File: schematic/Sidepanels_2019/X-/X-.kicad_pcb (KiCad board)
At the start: 2 copper layers, 327.5 x 83.1 mm, 33 parts, among them J1 Conn_01x04, J2 Conn_01x02

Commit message: First attempt at modifying to all Spectrolabs.  NOT COMPLETE
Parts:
- removed D1, D10, D11, D12, D13, D14, D2, D3, D4, D5, D6, D7, D8, D9: D_Schottky, CySat footprints:Toshiba_CUS08F30
- removed the SC1 at (206.5, 125.5)
- removed SC10, SC11, SC12, SC13, SC14, SC15, SC16, SC8, SC9: Solar_Cell, CySat footprints:TriSelectSolarPanel
- removed the SC2 at (81.2, 125.6)
- added SC3: Solar_Cell, CySat_Solar:Spectrolab, F.Cu at (191.8, 143.5)
- added SC4: Solar_Cell, CySat_Solar:Spectrolab, F.Cu at (370.8, 142.2)
- SC5, SC6, SC7: footprint CySat footprints:TriSelectSolarPanel -> CySat_Solar:Spectrolab
- moved SC7 115.9 mm to (279.4, 143.5), turned to 90 degrees
- moved D15 94.2 mm to (141.3, 180.7)
- moved J1 94.2 mm to (92.8, 149.1)
- moved J2 94.2 mm to (92.8, 138.1)
- moved SC1 91.1 mm to (102.9, 144.8)
- moved SC2 89.1 mm to (147.3, 142.2)
- moved SC5 72.7 mm to (234.9, 143.5), turned to 90 degrees
- moved SC6 61.7 mm to (325.0, 142.2)
- renumbered SC3 to SC1, SC4 to SC2
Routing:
- net VSS: track 386.0 -> 0.00 mm, vias 28 -> 0
- net Net-(D15-Pad1): track 71.2 -> 0.00 mm, vias 1 -> 0
- net Net-(D15-Pad2): track 65.2 -> 0.00 mm, vias 1 -> 0
- net VCC: track 56.3 -> 0.00 mm, vias 16 -> 0
- removed copper zone on F.Cu, net VCC
- removed copper zone on B.Cu, net VSS

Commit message: Updated X-
Updated X-, added 3D model, layout complete.  ERC and DRC pass
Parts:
- D15: footprint CySat footprints:Sun_Sensor -> Diode_SMD:D_0805_2012Metric
- SC1, SC2: footprint CySat footprints:Spectrolab -> CySat_Solar:Spectrolab
- moved SC7 1.80 mm to (280.7, 142.2)
- moved SC5 1.80 mm to (236.2, 142.2)
- moved SC3 1.27 mm to (191.8, 142.2)
- moved SC4 1.27 mm to (369.6, 142.2)
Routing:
- added copper zone on F.Cu, net VCC
- added copper zone on B.Cu, net VSS

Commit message: Update to X panels
Routing completed on both, solar panel change out complete on X+.  Re-did library and page settings.  DRC checks out.
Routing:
- net Net-(D15-Pad2): track 0.00 -> 69.5 mm, vias 0 -> 1
- net Net-(D15-Pad1): track 0.00 -> 67.7 mm, vias 0 -> 1
- net VSS: track 0.00 -> 47.5 mm, vias 0 -> 7
- net VCC: track 0.00 -> 25.0 mm, vias 0 -> 1

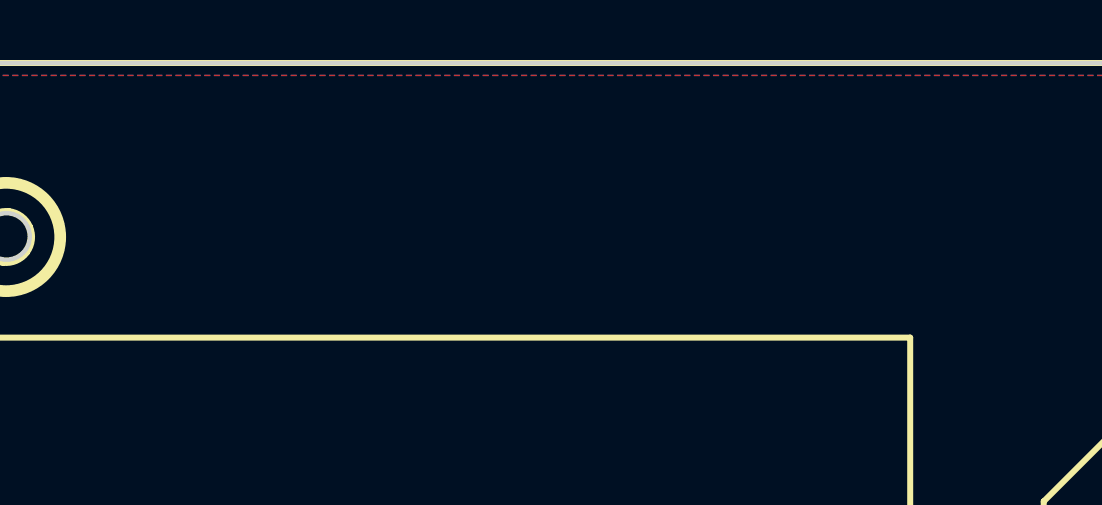
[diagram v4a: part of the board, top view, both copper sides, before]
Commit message: Update to all boards
Added labels to boards to resolve issue #2
Added names of students and faculty to boards
Generated Step files to resolve issue #4, please note the export does include the silkscreen.
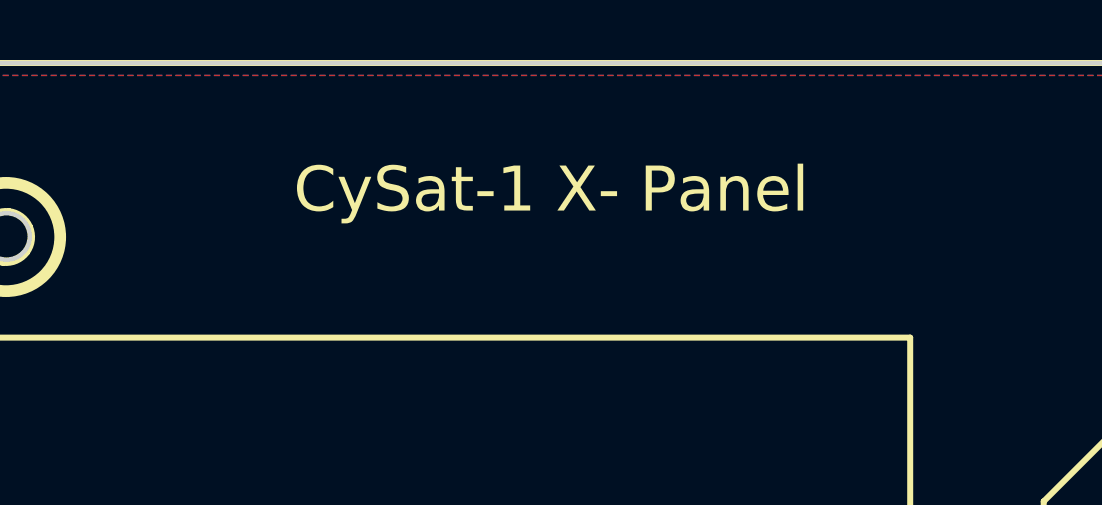
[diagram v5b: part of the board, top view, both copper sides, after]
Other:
- board text added: "CySat-1 X- Panel"
- board text added: "Special Thanks to our Donors:"

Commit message: Added cutout
Generated Gerber files
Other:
- outline, holes or cut-outs redrawn
- rule pad_to_mask_clearance: 0.051 -> 0

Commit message: Start on board changes
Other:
- net class Default removed

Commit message: Push of all changes made for June update
Major change was in the solar cell and creating a new library based on the old one.
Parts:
- SC1, SC2, SC3, SC4, SC5, SC6, SC7: footprint CySat_Solar:Spectrolab -> CySat:Spectrolabs_UTJ
- moved D15 81.4 mm to (103.1, 108.8)
- moved SC2 23.0 mm to (124.3, 141.7)
- moved SC1 22.6 mm to (80.3, 143.5)
- moved SC3 22.5 mm to (169.3, 141.7)
- moved SC5 21.9 mm to (214.3, 141.7)
- moved SC7 21.3 mm to (259.4, 141.6)
- moved SC6 20.9 mm to (304.1, 141.6)
- moved SC4 20.3 mm to (349.3, 141.7)
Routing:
- net VSS: track 47.5 -> 121.9 mm, vias 7 -> 14
- net Net-(D15-Pad1): track 67.7 -> 34.2 mm
- net Net-(D15-Pad2): track 69.5 -> 37.8 mm
- net VCC: track 25.0 -> 4.28 mm
